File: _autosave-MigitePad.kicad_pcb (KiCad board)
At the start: 2 copper layers, 139.7 x 134.1 mm, 76 parts, among them J1 OLED, J2 LED-Lily58-cache, SW1 SW_Push, SW2 Rotary_Encoder_Switch, U1 ProMicro

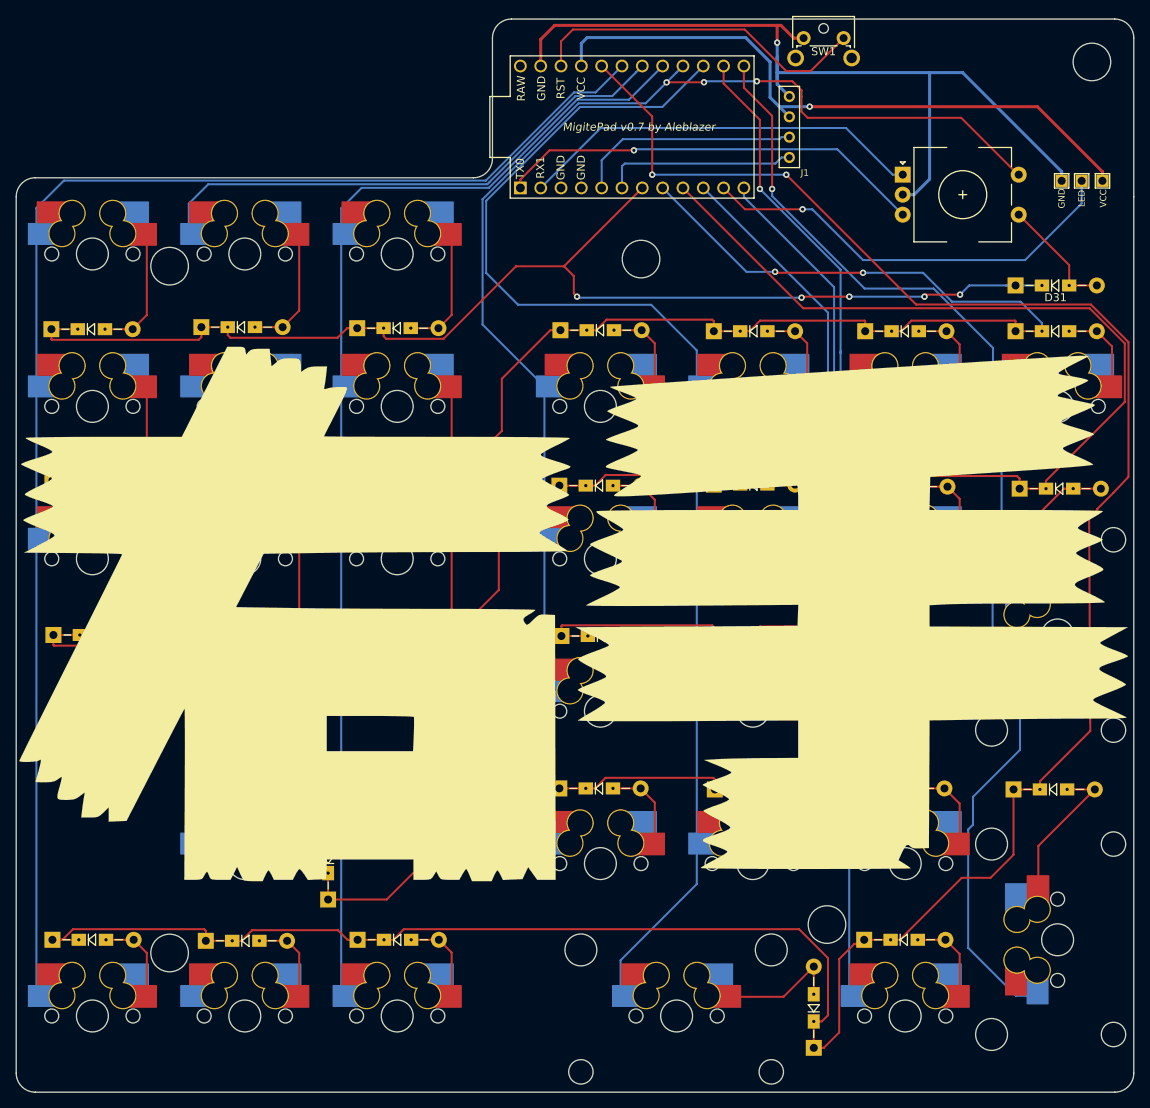
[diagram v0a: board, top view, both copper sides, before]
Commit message: Corrected Col1 Trace
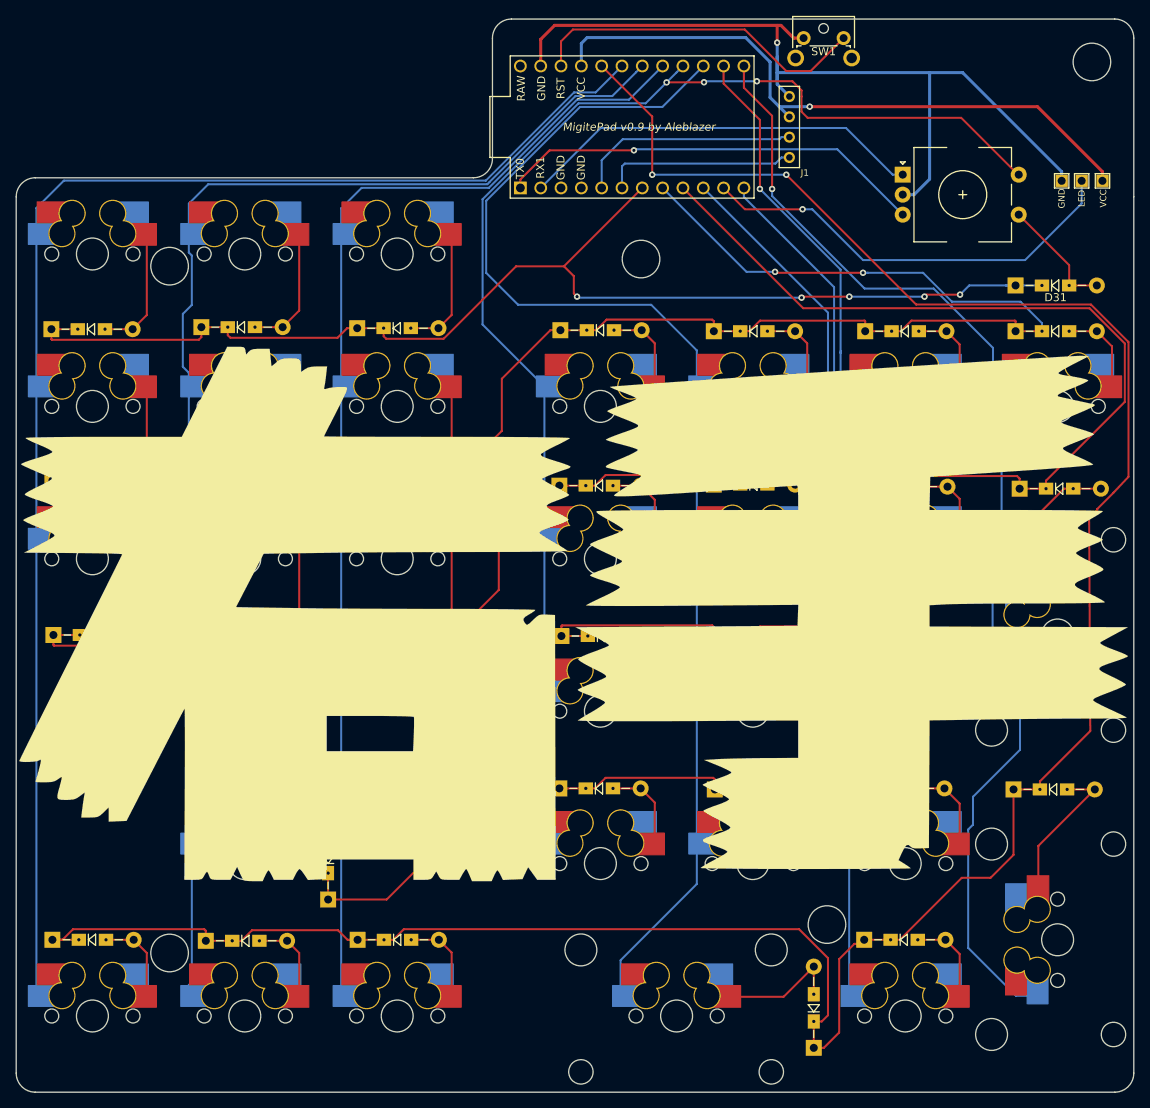
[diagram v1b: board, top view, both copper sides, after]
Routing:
- net COL1: track 67.6 -> 164.1 mm
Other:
- board text added: "MigitePad v0.9 by Aleblazer"
- board text removed: "MigitePad v0.7 by Aleblazer"
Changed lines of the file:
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@@
     (thickness 1.6)
     (drawings 22)
-    (tracks 552)
+    (tracks 568)
     (zones 0)
     (modules 76)
@@
       (net 53 RETX))
   )
-  (gr_text "MigitePad v0.7 by Aleblazer" (at 141.859 43.688) (layer F.SilkS)
+  (gr_text "MigitePad v0.9 by Aleblazer" (at 141.859 43.688) (layer F.SilkS)
     (effects (font (size 1 1) (thickness 0.15) italic))
   )
@@
   (segment (start 88.011 50.84402) (end 122.899047 50.84402) (width 0.254) (layer B.Cu) (net 37))
   (segment (start 122.899047 50.84402) (end 123.165 50.578066) (width 0.254) (layer B.Cu) (net 37))
+  (segment (start 85.583 57.063) (end 85.583 59.374742) (width 0.254) (layer B.Cu) (net 37))
+  (segment (start 85.962201 59.753943) (end 85.962201 65.929799) (width 0.254) (layer B.Cu) (net 37))
+  (segment (start 85.583 59.374742) (end 85.962201 59.753943) (width 0.254) (layer B.Cu) (net 37))
+  (segment (start 85.962201 65.929799) (end 84.836 67.056) (width 0.254) (layer B.Cu) (net 37))
+  (segment (start 84.836 67.056) (end 84.836 73.66) (width 0.254) (layer B.Cu) (net 37))
+  (segment (start 85.583 74.407) (end 85.583 76.113) (width 0.254) (layer B.Cu) (net 37))
+  (segment (start 84.836 73.66) (end 85.583 74.407) (width 0.254) (layer B.Cu) (net 37))
+  (segment (start 85.583 77.488) (end 85.583 95.163) (width 0.254) (layer B.Cu) (net 37))
+  (segment (start 85.583 76.113) (end 85.583 77.488) (width 0.254) (layer B.Cu) (net 37))
+  (segment (start 85.583 96.538) (end 85.583 133.263) (width 0.254) (layer B.Cu) (net 37))
+  (segment (start 85.583 95.163) (end 85.583 96.538) (width 0.254) (layer B.Cu) (net 37))
+  (segment (start 85.583 150.938) (end 85.583 152.313) (width 0.254) (layer B.Cu) (net 37))
+  (segment (start 85.962201 150.558799) (end 85.583 150.938) (width 0.254) (layer B.Cu) (net 37))
+  (segment (start 85.583 134.638) (end 85.962201 135.017201) (width 0.254) (layer B.Cu) (net 37))
+  (segment (start 85.962201 135.017201) (end 85.962201 150.558799) (width 0.254) (layer B.Cu) (net 37))
+  (segment (start 85.583 133.263) (end 85.583 134.638) (width 0.254) (layer B.Cu) (net 37))
   (segment (start 104.633 57.063) (end 104.633 152.313) (width 0.254) (layer B.Cu) (net 38))
   (segment (start 140.60173 40.27802) (end 144.81175 36.068) (width 0.254) (layer B.Cu) (net 38))
